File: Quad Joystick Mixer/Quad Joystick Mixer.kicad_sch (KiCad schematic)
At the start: 0 parts

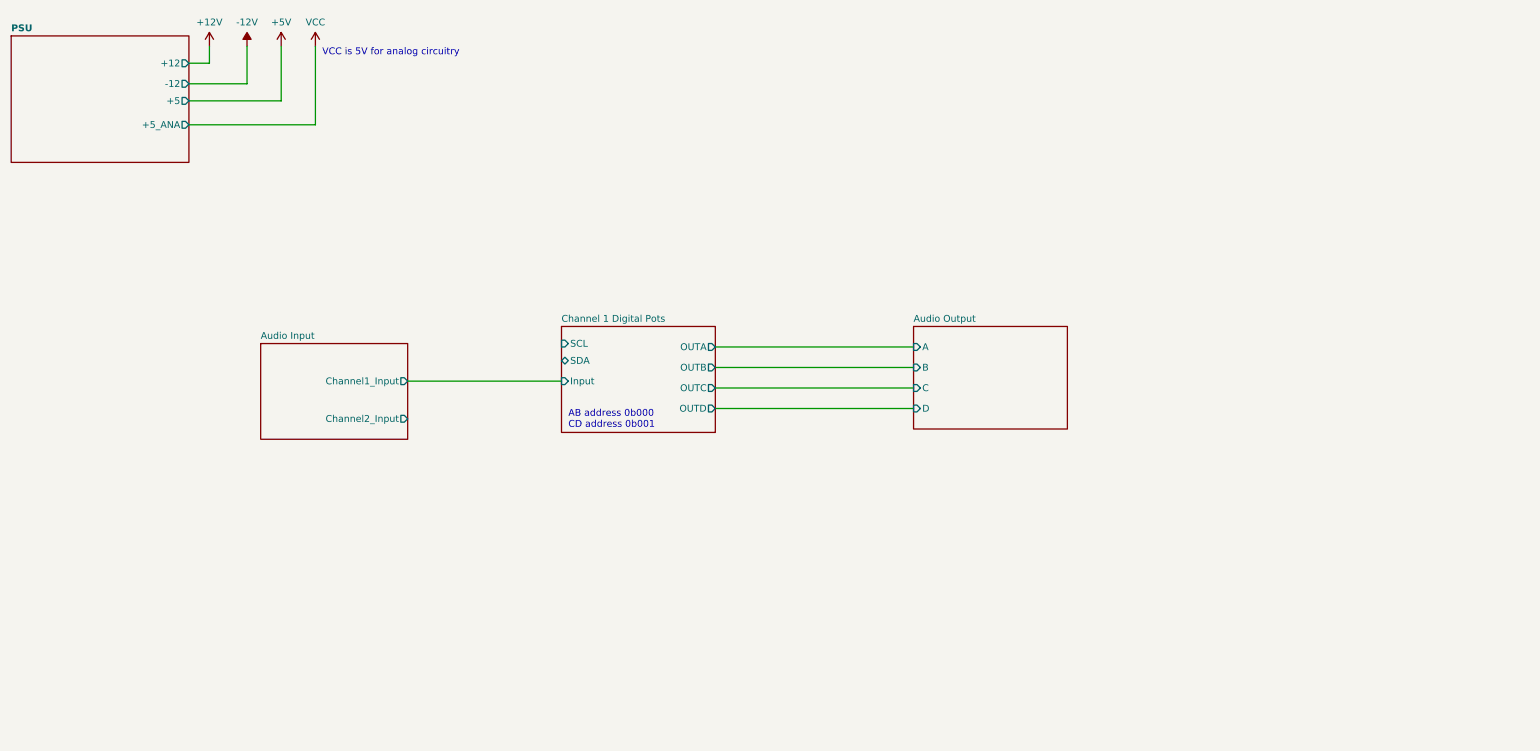
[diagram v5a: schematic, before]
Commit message: create joystick conditioning circuit
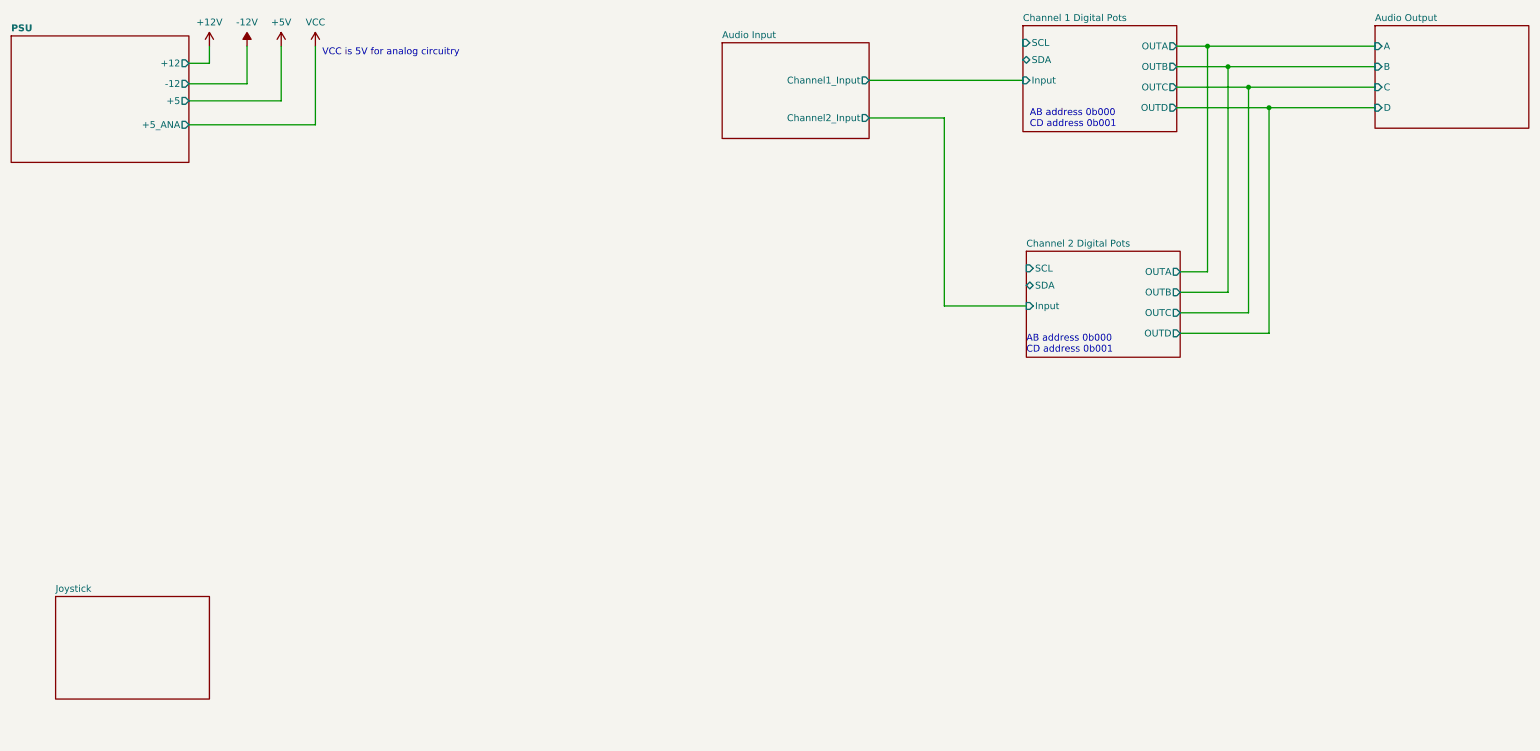
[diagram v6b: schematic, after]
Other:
- added sheet Channel 2 Digital Pots (digitalPot.kicad_sch)
- added sheet Joystick (joystick.kicad_sch)
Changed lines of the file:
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@@
     (rev "P1")
   )
+  (junction (at 279.4 67.945) (diameter 0) (color 0 0 0 0)
+  )
+  (junction (at 290.83 79.375) (diameter 0) (color 0 0 0 0)
+  )
+  (junction (at 287.02 75.565) (diameter 0) (color 0 0 0 0)
+  )
+  (junction (at 283.21 71.755) (diameter 0) (color 0 0 0 0)
+  )
+  (wire (pts (xy 230.505 116.205) (xy 245.745 116.205))
+    (stroke (width 0) (type default))
+  )
+  (wire (pts (xy 230.505 81.28) (xy 230.505 116.205))
+    (stroke (width 0) (type default))
+  )
+  (wire (pts (xy 279.4 67.945) (xy 310.515 67.945))
+    (stroke (width 0) (type default))
+  )
   (wire (pts (xy 90.17 82.55) (xy 113.665 82.55))
     (stroke (width 0) (type default))
   )
-  (wire (pts (xy 187.96 131.445) (xy 224.79 131.445))
-    (stroke (width 0) (type default))
-  )
-  (wire (pts (xy 130.81 130.175) (xy 159.385 130.175))
+  (wire (pts (xy 274.32 109.855) (xy 279.4 109.855))
+    (stroke (width 0) (type default))
+  )
+  (wire (pts (xy 273.685 75.565) (xy 287.02 75.565))
+    (stroke (width 0) (type default))
+  )
+  (wire (pts (xy 216.535 74.295) (xy 245.11 74.295))
+    (stroke (width 0) (type default))
+  )
+  (wire (pts (xy 287.02 75.565) (xy 310.515 75.565))
+    (stroke (width 0) (type default))
+  )
+  (wire (pts (xy 274.32 117.475) (xy 287.02 117.475))
     (stroke (width 0) (type default))
   )
@@
     (stroke (width 0) (type default))
   )
+  (wire (pts (xy 279.4 109.855) (xy 279.4 67.945))
+    (stroke (width 0) (type default))
+  )
+  (wire (pts (xy 274.32 113.665) (xy 283.21 113.665))
+    (stroke (width 0) (type default))
+  )
+  (wire (pts (xy 216.535 81.28) (xy 230.505 81.28))
+    (stroke (width 0) (type default))
+  )
   (wire (pts (xy 107.315 78.105) (xy 107.315 67.945))
     (stroke (width 0) (type default))
   )
-  (wire (pts (xy 187.96 123.825) (xy 224.79 123.825))
+  (wire (pts (xy 283.21 71.755) (xy 310.515 71.755))
+    (stroke (width 0) (type default))
+  )
+  (wire (pts (xy 273.685 67.945) (xy 279.4 67.945))
     (stroke (width 0) (type default))
   )
@@
     (stroke (width 0) (type default))
   )
+  (wire (pts (xy 274.32 121.285) (xy 290.83 121.285))
+    (stroke (width 0) (type default))
+  )
+  (wire (pts (xy 290.83 121.285) (xy 290.83 79.375))
+    (stroke (width 0) (type default))
+  )
   (wire (pts (xy 93.98 71.12) (xy 93.98 67.945))
     (stroke (width 0) (type default))
@@
     (stroke (width 0) (type default))
   )
-  (wire (pts (xy 187.96 135.255) (xy 224.79 135.255))
-    (stroke (width 0) (type default))
-  )
-  (wire (pts (xy 187.96 127.635) (xy 224.79 127.635))
+  (wire (pts (xy 287.02 117.475) (xy 287.02 75.565))
+    (stroke (width 0) (type default))
+  )
+  (wire (pts (xy 290.83 79.375) (xy 310.515 79.375))
+    (stroke (width 0) (type default))
+  )
+  (wire (pts (xy 273.685 79.375) (xy 290.83 79.375))
+    (stroke (width 0) (type default))
+  )
+  (wire (pts (xy 273.685 71.755) (xy 283.21 71.755))
+    (stroke (width 0) (type default))
+  )
+  (wire (pts (xy 283.21 113.665) (xy 283.21 71.755))
     (stroke (width 0) (type default))
   )
@@
     )
   )
-  (text "AB address 0b000\nCD address 0b001" (at 160.655 139.065 0)
+  (text "AB address 0b000\nCD address 0b001" (at 246.38 83.185 0)
     (effects (font (size 1.27 1.27)) (justify left bottom))
   )
   (text "VCC is 5V for analog circuitry" (at 114.935 69.85 0)
+    (effects (font (size 1.27 1.27)) (justify left bottom))
+  )
+  (text "AB address 0b000\nCD address 0b001" (at 245.745 125.095 0)
     (effects (font (size 1.27 1.27)) (justify left bottom))
   )
@@
     )
   )
-  (sheet (at 159.385 120.015) (size 28.575 19.685) (fields_autoplaced)
+  (sheet (at 65.405 170.18) (size 28.575 19.05) (fields_autoplaced)
     (stroke (width 0.1524) (type solid))
     (fill (color 0 0 0 0.0000))
-    (property "Sheetname" "Channel 1 Digital Pots" (at 159.385 119.3034 0)
+    (property "Sheetname" "Joystick" (at 65.405 169.4684 0)
       (effects (font (size 1.27 1.27)) (justify left bottom))
     )
-    (property "Sheetfile" "digitalPot.kicad_sch" (at 159.385 140.2846 0)
+    (property "Sheetfile" "joystick.kicad_sch" (at 65.405 189.8146 0)
       (effects (font (size 1.27 1.27)) (justify left top) hide)
     )
-    (pin "Input" input (at 159.385 130.175 180)
+    (instances
+      (project "Quad Joystick Mixer"
+        (path "/e9da4955-68c1-4335-ab8e-8a9cc0328d2d" (page "7"))
+      )
+    )
+  )
+  (sheet (at 245.11 64.135) (size 28.575 19.685) (fields_autoplaced)
+    (stroke (width 0.1524) (type solid))
+    (fill (color 0 0 0 0.0000))
+    (property "Sheetname" "Channel 1 Digital Pots" (at 245.11 63.4234 0)
+      (effects (font (size 1.27 1.27)) (justify left bottom))
+    )
+    (property "Sheetfile" "digitalPot.kicad_sch" (at 245.11 84.4046 0)
+      (effects (font (size 1.27 1.27)) (justify left top) hide)
+    )
+    (pin "Input" input (at 245.11 74.295 180)
       (effects (font (size 1.27 1.27)) (justify left))
     )
-    (pin "SDA" bidirectional (at 159.385 126.365 180)
+    (pin "SDA" bidirectional (at 245.11 70.485 180)
       (effects (font (size 1.27 1.27)) (justify left))
     )
-    (pin "SCL" input (at 159.385 123.19 180)
+    (pin "SCL" input (at 245.11 67.31 180)
       (effects (font (size 1.27 1.27)) (justify left))
     )
-    (pin "OUTA" output (at 187.96 123.825 0)
-      (effects (font (size 1.27 1.27)) (justify right))
-    )
-    (pin "OUTB" output (at 187.96 127.635 0)
-      (effects (font (size 1.27 1.27)) (justify right))
-    )
-    (pin "OUTD" output (at 187.96 135.255 0)
-      (effects (font (size 1.27 1.27)) (justify right))
-    )
-    (pin "OUTC" output (at 187.96 131.445 0)
+    (pin "OUTA" output (at 273.685 67.945 0)
+      (effects (font (size 1.27 1.27)) (justify right))
+    )
+    (pin "OUTB" output (at 273.685 71.755 0)
+      (effects (font (size 1.27 1.27)) (justify right))
+    )
+    (pin "OUTD" output (at 273.685 79.375 0)
+      (effects (font (size 1.27 1.27)) (justify right))
+    )
+    (pin "OUTC" output (at 273.685 75.565 0)
       (effects (font (size 1.27 1.27)) (justify right))
     )
@@
     )
   )
-  (sheet (at 224.79 120.015) (size 28.575 19.05) (fields_autoplaced)
+  (sheet (at 245.745 106.045) (size 28.575 19.685) (fields_autoplaced)
     (stroke (width 0.1524) (type solid))
     (fill (color 0 0 0 0.0000))
-    (property "Sheetname" "Audio Output" (at 224.79 119.3034 0)
+    (property "Sheetname" "Channel 2 Digital Pots" (at 245.745 105.3334 0)
       (effects (font (size 1.27 1.27)) (justify left bottom))
     )
-    (property "Sheetfile" "audioOutput.kicad_sch" (at 224.79 139.6496 0)
+    (property "Sheetfile" "digitalPot.kicad_sch" (at 245.745 126.3146 0)
       (effects (font (size 1.27 1.27)) (justify left top) hide)
     )
-    (pin "A" input (at 224.79 123.825 180)
+    (pin "Input" input (at 245.745 116.205 180)
       (effects (font (size 1.27 1.27)) (justify left))
     )
-    (pin "B" input (at 224.79 127.635 180)
+    (pin "SDA" bidirectional (at 245.745 112.395 180)
       (effects (font (size 1.27 1.27)) (justify left))
     )
-    (pin "C" input (at 224.79 131.445 180)
+    (pin "SCL" input (at 245.745 109.22 180)
       (effects (font (size 1.27 1.27)) (justify left))
     )
-    (pin "D" input (at 224.79 135.255 180)
+    (pin "OUTA" output (at 274.32 109.855 0)
+      (effects (font (size 1.27 1.27)) (justify right))
+    )
+    (pin "OUTB" output (at 274.32 113.665 0)
+      (effects (font (size 1.27 1.27)) (justify right))
+    )
+    (pin "OUTD" output (at 274.32 121.285 0)
+      (effects (font (size 1.27 1.27)) (justify right))
+    )
+    (pin "OUTC" output (at 274.32 117.475 0)
+      (effects (font (size 1.27 1.27)) (justify right))
+    )
+    (instances
+      (project "Quad Joystick Mixer"
+        (path "/e9da4955-68c1-4335-ab8e-8a9cc0328d2d" (page "6"))
+      )
+    )
+  )
+  (sheet (at 310.515 64.135) (size 28.575 19.05) (fields_autoplaced)
+    (stroke (width 0.1524) (type solid))
+    (fill (color 0 0 0 0.0000))
+    (property "Sheetname" "Audio Output" (at 310.515 63.4234 0)
+      (effects (font (size 1.27 1.27)) (justify left bottom))
+    )
+    (property "Sheetfile" "audioOutput.kicad_sch" (at 310.515 83.7696 0)
+      (effects (font (size 1.27 1.27)) (justify left top) hide)
+    )
+    (pin "A" input (at 310.515 67.945 180)
+      (effects (font (size 1.27 1.27)) (justify left))
+    )
+    (pin "B" input (at 310.515 71.755 180)
+      (effects (font (size 1.27 1.27)) (justify left))
+    )
+    (pin "C" input (at 310.515 75.565 180)
+      (effects (font (size 1.27 1.27)) (justify left))
+    )
+    (pin "D" input (at 310.515 79.375 180)
       (effects (font (size 1.27 1.27)) (justify left))
     )
@@
     )
   )
-  (sheet (at 103.505 123.19) (size 27.305 17.78) (fields_autoplaced)
+  (sheet (at 189.23 67.31) (size 27.305 17.78) (fields_autoplaced)
     (stroke (width 0.1524) (type solid))
     (fill (color 0 0 0 0.0000))
-    (property "Sheetname" "Audio Input" (at 103.505 122.4784 0)
+    (property "Sheetname" "Audio Input" (at 189.23 66.5984 0)
       (effects (font (size 1.27 1.27)) (justify left bottom))
     )
-    (property "Sheetfile" "audioInput.kicad_sch" (at 103.505 141.5546 0)
+    (property "Sheetfile" "audioInput.kicad_sch" (at 189.23 85.6746 0)
       (effects (font (size 1.27 1.27)) (justify left top) hide)
     )
-    (pin "Channel2_Input" output (at 130.81 137.16 0)
-      (effects (font (size 1.27 1.27)) (justify right))
-    )
-    (pin "Channel1_Input" output (at 130.81 130.175 0)
-      (effects (font (size 1.27 1.27)) (justify right))
-    )
+    (pin "Channel2_Input" output (at 216.535 81.28 0)
+      (effects (font (size 1.27 1.27)) (justify right))
+    )
+    (pin "Channel1_Input" output (at 216.535 74.295 0)
+      (effects (font (size 1.27 1.27)) (justify right))
+    )

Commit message: progress on schematic
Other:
- added sheet Teensy (teensy.kicad_sch)
- sheet Joystick ports: added AB_control, CD_control; removed none
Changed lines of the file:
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@@
       (effects (font (size 1.27 1.27)) (justify left top) hide)
+    )
+    (pin "CD_control" output (at 93.98 182.88 0)
+      (effects (font (size 1.27 1.27)) (justify right))
+    )
+    (pin "AB_control" output (at 93.98 177.165 0)
+      (effects (font (size 1.27 1.27)) (justify right))
     )
     (instances
@@
       )
     )
+  )
+  (sheet (at 286.385 182.245) (size 23.495 14.605) (fields_autoplaced)
+    (stroke (width 0.1524) (type solid))
+    (fill (color 0 0 0 0.0000))
+    (property "Sheetname" "Teensy" (at 286.385 181.5334 0)
+      (effects (font (size 1.27 1.27)) (justify left bottom))
+    )
+    (property "Sheetfile" "teensy.kicad_sch" (at 286.385 197.4346 0)
+      (effects (font (size 1.27 1.27)) (justify left top) hide)
+    )
+    (instances
+      (project "Quad Joystick Mixer"
+        (path "/e9da4955-68c1-4335-ab8e-8a9cc0328d2d" (page "8"))
+      )
+    )

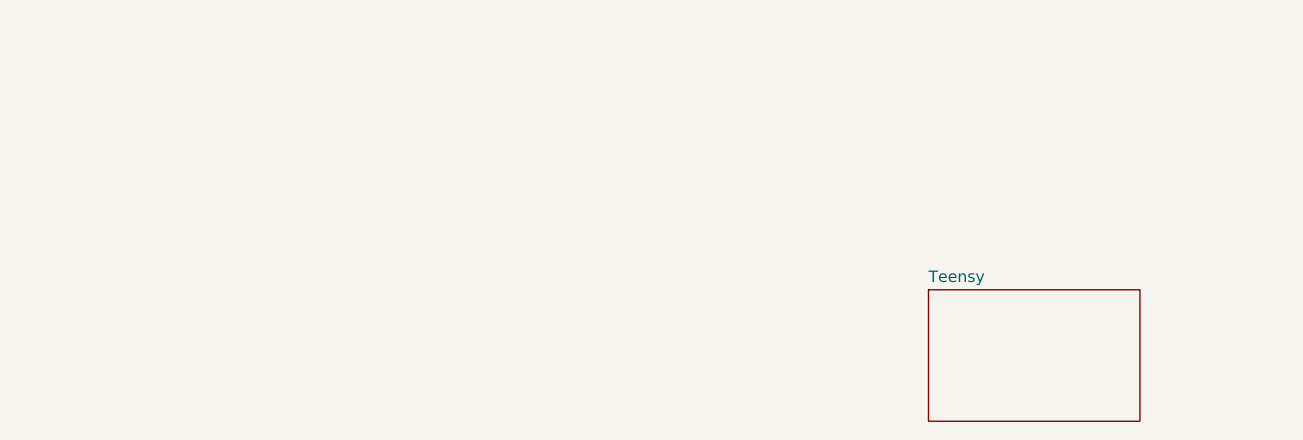
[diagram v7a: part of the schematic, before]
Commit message: add in rotary circuit and some docs
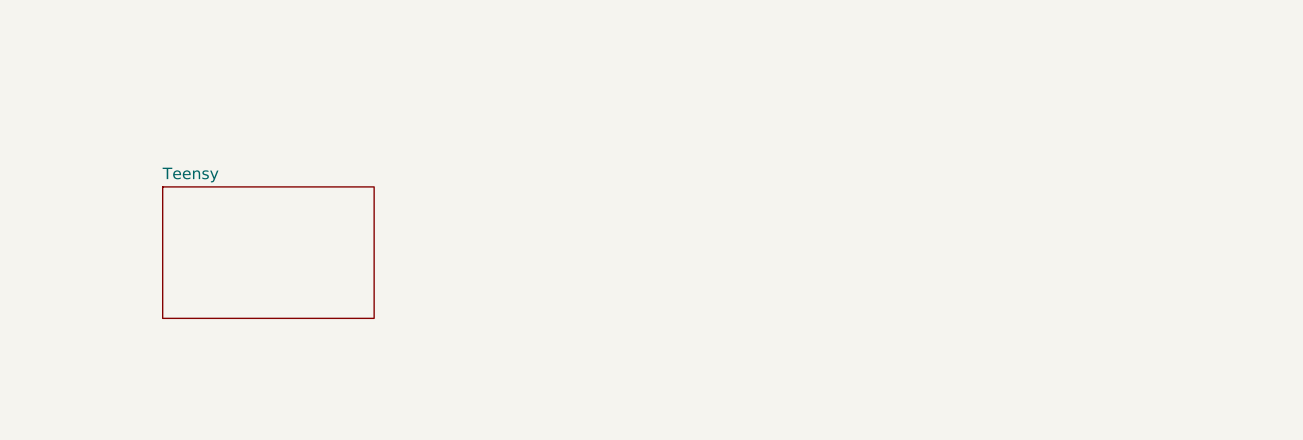
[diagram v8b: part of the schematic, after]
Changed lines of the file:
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@@
   (title_block
     (title "Quadrophonic Joystick Mixer")
-    (date "2024-02-02")
+    (date "2024-02-14")
     (rev "P1")
   )
@@
     )
   )
-  (sheet (at 286.385 182.245) (size 23.495 14.605) (fields_autoplaced)
+  (sheet (at 201.295 170.815) (size 23.495 14.605) (fields_autoplaced)
     (stroke (width 0.1524) (type solid))
     (fill (color 0 0 0 0.0000))
-    (property "Sheetname" "Teensy" (at 286.385 181.5334 0)
+    (property "Sheetname" "Teensy" (at 201.295 170.1034 0)
       (effects (font (size 1.27 1.27)) (justify left bottom))
     )
-    (property "Sheetfile" "teensy.kicad_sch" (at 286.385 197.4346 0)
+    (property "Sheetfile" "teensy.kicad_sch" (at 201.295 186.0046 0)
       (effects (font (size 1.27 1.27)) (justify left top) hide)
     )
